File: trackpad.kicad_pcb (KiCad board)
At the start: 2 copper layers, 172 x 152.9 mm, 103 parts, among them J1 USB_C_Receptacle_USB2.0, J10 Conn_01x01_Pin, J3 Conn_01x03, J5 Conn_01x07_Pin, J6 Conn_01x04_Pin, J7 Conn_01x02_Pin, J8 Conn_01x08_Pin, J9 Conn_01x02_Pin, SW1 RotaryEncoder_Switch, SW2 SW_Push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

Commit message: Tweak fills.
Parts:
- moved R15 5.89 mm to (24.0, 167.1)
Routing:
- net /Sensor/VIK_RGB: track 41.5 -> 39.9 mm
- net Net-(LED6-DIN): track 2.65 -> 4.18 mm
- net VCC: track 87.2 -> 86.4 mm, vias 4 -> 3
- net GND2: vias 68 -> 70
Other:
- board text added: "DIN VCC GP4 CHANGE SDA SCL +3.3V GND"
- board text removed: "DOUT VCC GP4 CHANGE SDA SCL +3.3V GND"

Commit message: Minor tweaks
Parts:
- removed R4, R5: 4.7k, Resistor_SMD:R_1206_3216Metric_Pad1.30x1.75mm_HandSolder
- added C37: 100n, Capacitor_SMD:C_0402_1005Metric, F.Cu at (48.1, 180.0)
- moved SW_BOOT1 15.7 mm to (52.4, 179.3)
- moved J7 2.79 mm to (88.0, 185.3)
- moved U7 2.69 mm to (74.4, 183.8), turned to 0 degrees
- moved J6 2.47 mm to (38.9, 175.1)
- moved R7 1.13 mm to (73.2, 181.8)
- moved C7 0.99 mm to (39.6, 177.8), turned to 0 degrees
- moved R6 0.73 mm to (79.4, 182.7)
- moved R17 0.58 mm to (95.4, 178.4)
- moved C6 0.52 mm to (42.6, 177.3)
- moved C30 0.51 mm to (68.2, 187.6)
- moved U3 0.50 mm to (70.7, 187.1)
- moved J1 0.45 mm to (76.7, 175.1)
- moved C14 0.40 mm to (95.5, 175.6)
- moved R1 0.25 mm to (47.9, 175.9)
- moved C20 0.20 mm to (107.5, 173.4)
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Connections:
- U1 pad 12: unconnected-(U1-GPIO9-Pad12) -> /Macropad/SDA
- U1 pad 13: unconnected-(U1-GPIO10-Pad13) -> /Macropad/SCL
- U1 pad 6: /Macropad/SDA -> unconnected-(U1-GPIO4-Pad6)
- U1 pad 7: /Macropad/SCL -> unconnected-(U1-GPIO5-Pad7)
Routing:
- net Net-(R2-Pad1): track 21.9 -> 4.47 mm
- net /Macropad/D+: track 40.9 -> 37.3 mm
- net GND2: track 61.7 -> 65.1 mm, vias 70 -> 73
- net +3.3V: track 101.1 -> 98.0 mm
- net VBUS: track 14.4 -> 17.1 mm
- net /Macropad/VIK_RGB: track 119.3 -> 116.9 mm
- net /Macropad/D-: track 40.3 -> 38.3 mm
- net /Macropad/GPIO_AD2: track 86.8 -> 88.2 mm
- net VCC: track 86.4 -> 87.8 mm
- net GND: track 30.6 -> 31.8 mm, vias 58 -> 60
- net /Macropad/SCL: track 39.9 -> 38.8 mm, vias 3 -> 0
- net /Macropad/MISO: track 25.0 -> 24.0 mm
- net /Macropad/SPI_CS: track 26.3 -> 25.3 mm
- net /Macropad/GPIO_AD1: track 87.5 -> 88.5 mm
- net /Macropad/MOSI: track 28.9 -> 27.9 mm
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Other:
- board text added: "LED6"
- board text added: "SDA SCL VCC GND"
- board text removed: "SDA SCL VDD GND"
- board text removed: "SW7"

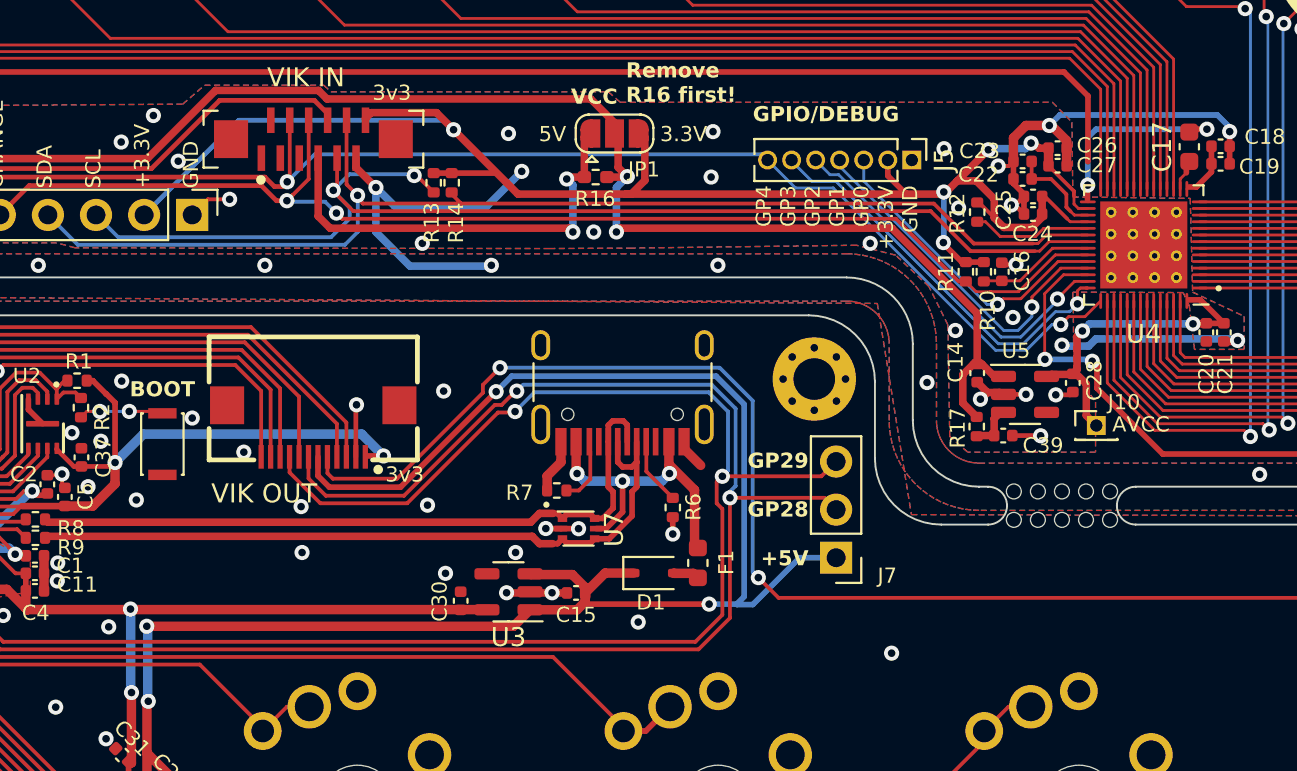
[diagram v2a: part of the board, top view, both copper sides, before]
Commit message: Add missing paste on max touch epad.
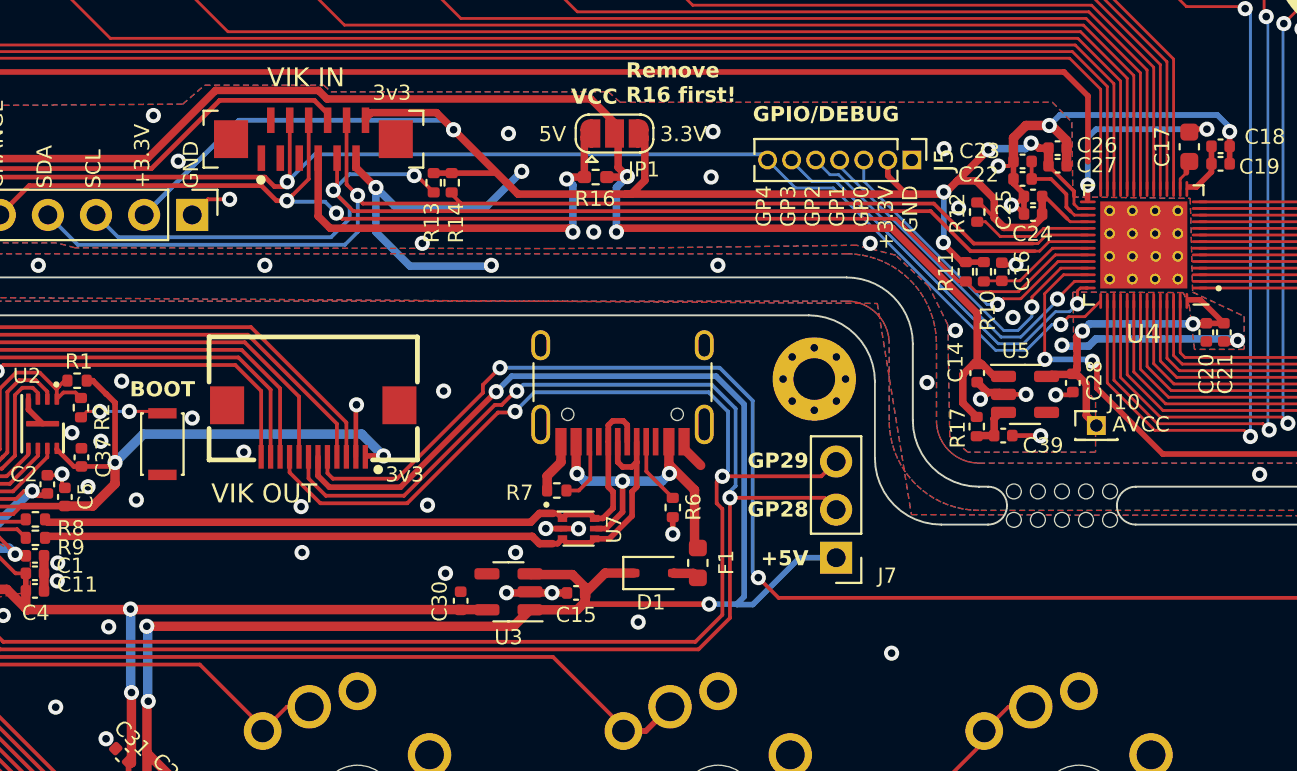
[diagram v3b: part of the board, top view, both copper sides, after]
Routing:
- net GND2: vias 73 -> 72
